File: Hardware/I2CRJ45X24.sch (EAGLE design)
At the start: 82 parts, among them IC1 MCP23017SO, IC2 MCP23017SO, IC3 MCP23017SO, IC4 MCP23017SO, IC5 MCP23017SO, IC6 MCP23017SO, J1 I2C-BREAKOUT, J2 I2C-BREAKOUT, J3 M01-PLAIN, J4 RJ45-X8, J5 RJ45-X8, J6 RJ45-X8

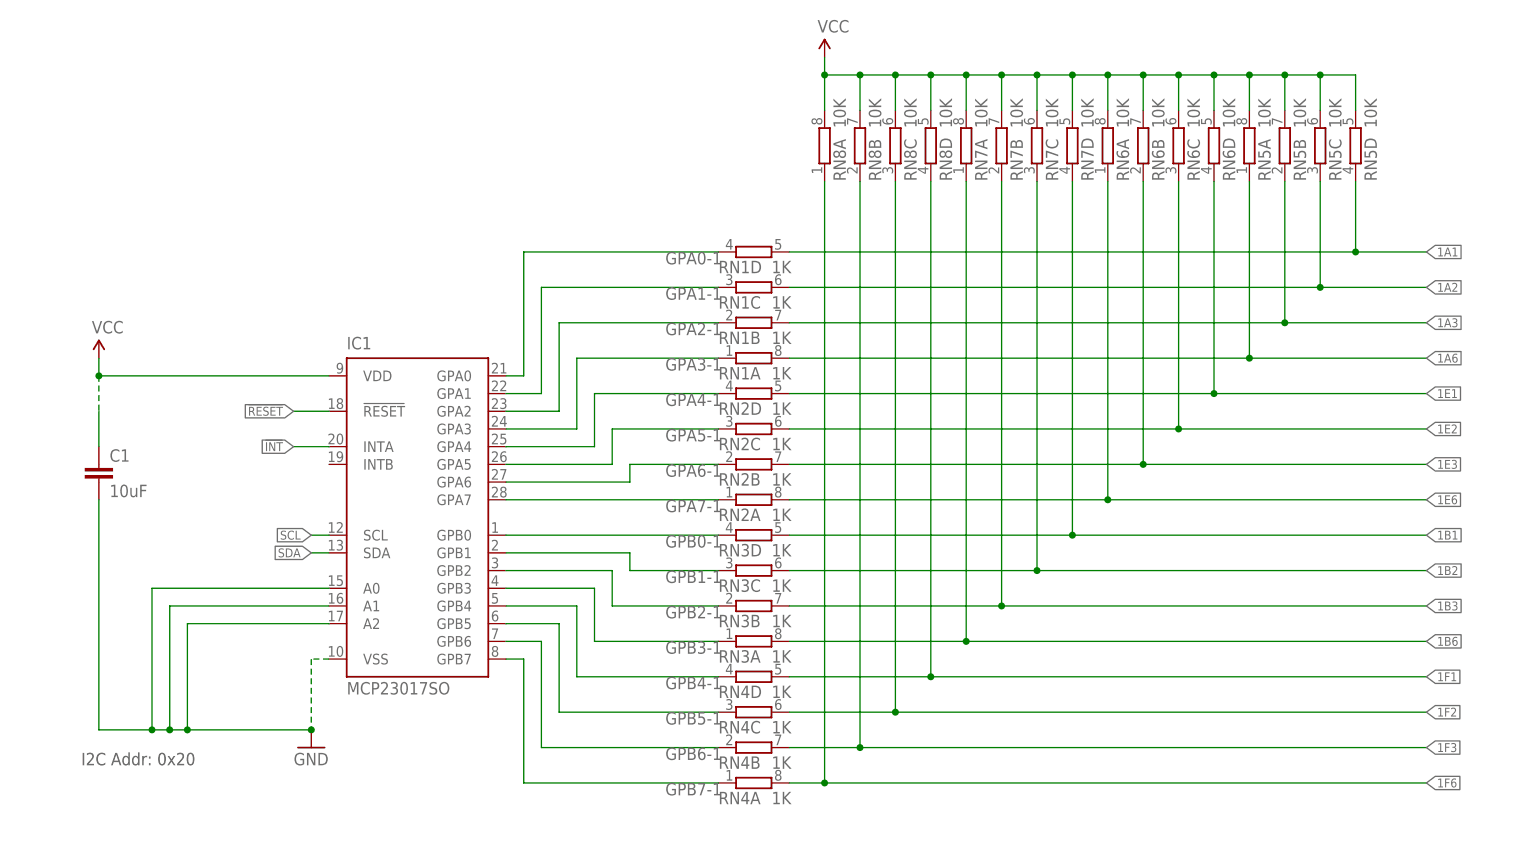
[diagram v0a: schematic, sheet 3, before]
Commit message: Major rework: rerouted entire board.
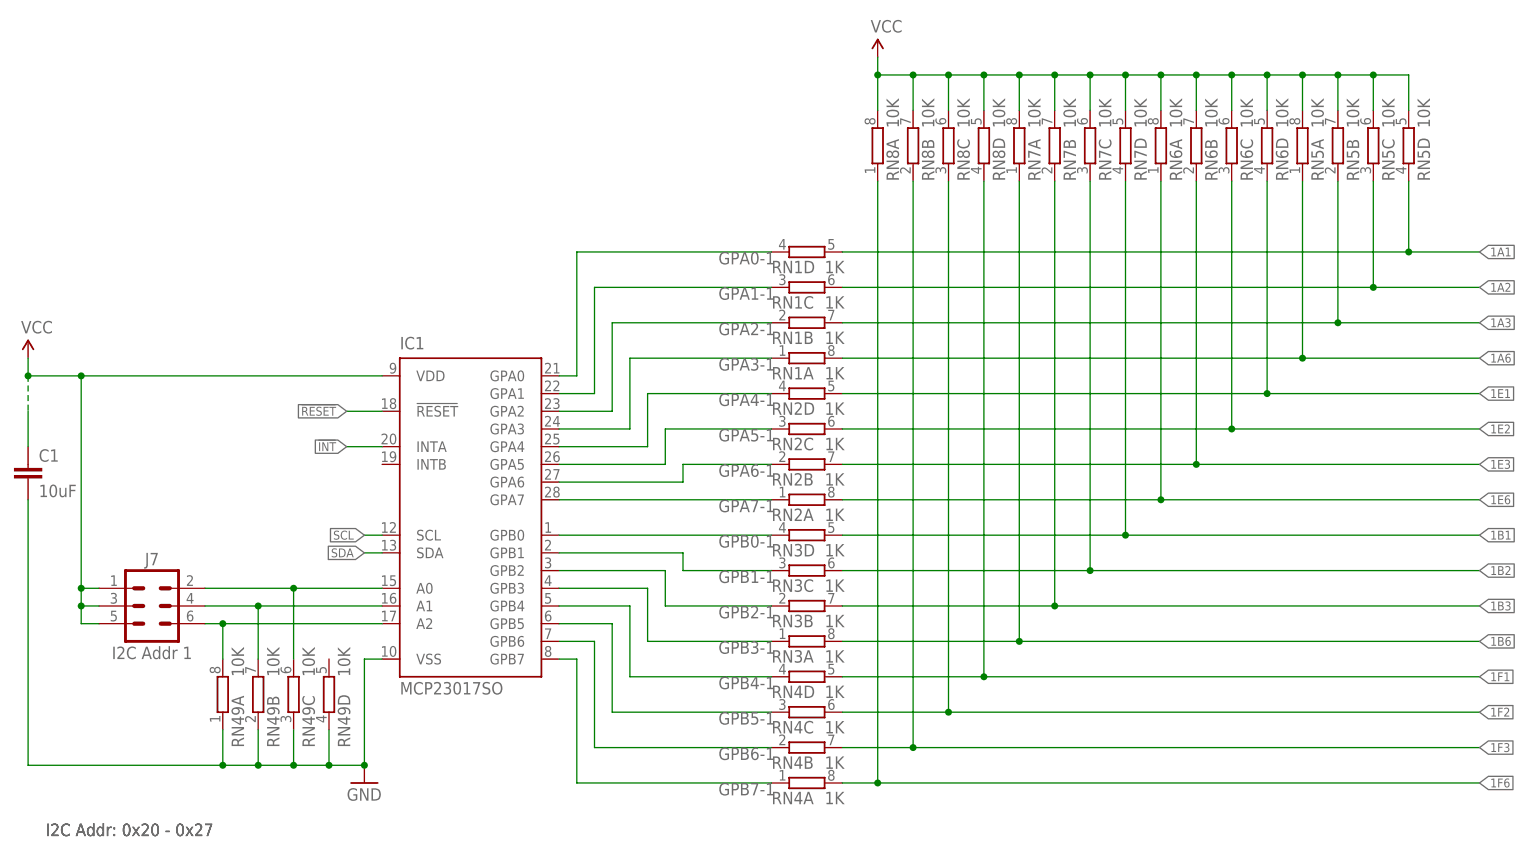
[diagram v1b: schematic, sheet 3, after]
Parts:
- added J10: I2C Addr 4, SuperHouse-Connectors:M02X3-PIN
- added J11: I2C Addr 3, SuperHouse-Connectors:M02X3-PIN
- added J12: I2C Addr 2, SuperHouse-Connectors:M02X3-PIN
- added J7: I2C Addr 1, SuperHouse-Connectors:M02X3-PIN
- added J8: I2C Addr 6, SuperHouse-Connectors:M02X3-PIN
- added J9: I2C Addr 5, SuperHouse-Connectors:M02X3-PIN
- added RN49, RN50, RN51, RN52, RN53, RN54: 10K, SuperHouse-Resistors:4R-NCAY16
- SJ1, SJ2: device SuperHouse-Jumpers:SJ-NORMAL -> SuperHouse-Connectors:M02-PIN
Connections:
- new net N$10: IC2.A1, J12.4, RN50B.2
- new net N$11: IC2.A2, J12.6, RN50A.2
- new net N$12: IC3.A2, J11.6, RN51A.2
- new net N$13: IC3.A0, J11.2, RN51C.2
- new net N$14: IC3.A1, J11.4, RN51B.2
- new net N$15: IC4.A2, J10.6, RN52A.2
- new net N$16: IC4.A0, J10.2, RN52C.2
- new net N$17: IC4.A1, J10.4, RN52B.2
- new net N$18: IC5.A2, J9.6, RN53A.2
- new net N$19: IC5.A0, J9.2, RN53C.2
- new net N$20: IC5.A1, J9.4, RN53B.2
- new net N$21: IC6.A2, J8.6, RN54A.2
- new net N$22: IC6.A0, J8.2, RN54C.2
- new net N$23: IC6.A1, J8.4, RN54B.2
- new net N$4: IC1.A2, J7.6, RN49A.2
- new net N$5: IC1.A1, J7.4, RN49B.2
- new net N$6: IC1.A0, J7.2, RN49C.2
- new net N$9: IC2.A0, J12.2, RN50C.2
- net GND: now also RN49A.1, RN49B.1, RN49C.1, RN49D.1, RN50A.1, RN50B.1, RN50C.1, RN50D.1, RN51A.1, RN51B.1, RN51C.1, RN51D.1, RN52A.1, RN52B.1, RN52C.1, RN52D.1, RN53A.1, RN53B.1, RN53C.1, RN53D.1, RN54A.1, RN54B.1, RN54C.1, RN54D.1; no longer IC1.A0, IC1.A1, IC1.A2, IC2.A1, IC2.A2, IC3.A0, IC3.A2, IC4.A2, IC5.A0, IC5.A1, IC6.A1
- net VCC: now also J10.1, J10.3, J10.5, J11.1, J11.3, J11.5, J12.1, J12.3, J12.5, J7.1, J7.3, J7.5, J8.1, J8.3, J8.5, J9.1, J9.3, J9.5; no longer IC2.A0, IC3.A1, IC4.A0, IC4.A1, IC5.A2, IC6.A0, IC6.A2
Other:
- note added: "I2C Addr: 0x20 - 0x27"
- note added: "I2C Addresses: 0x20-0x27"
- note added: "V3.0 (2021-06-08)"
- note removed: "I2C Addr: 0x20"
- note removed: "I2C Addr: 0x21"
- note removed: "I2C Addr: 0x22"
- note removed: "I2C Addr: 0x23"
- note removed: "I2C Addr: 0x24"
- note removed: "I2C Addr: 0x25"
- note removed: "I2C Addresses: 0x20-0x25"
- note removed: "V3.0 (2021-06-04)"
- moved on the sheet: C1, C2, C3, C4, C5, C6, C7, C8, C9, IC1, IC2, IC3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
